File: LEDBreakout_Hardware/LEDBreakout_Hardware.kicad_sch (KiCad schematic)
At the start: 17 parts

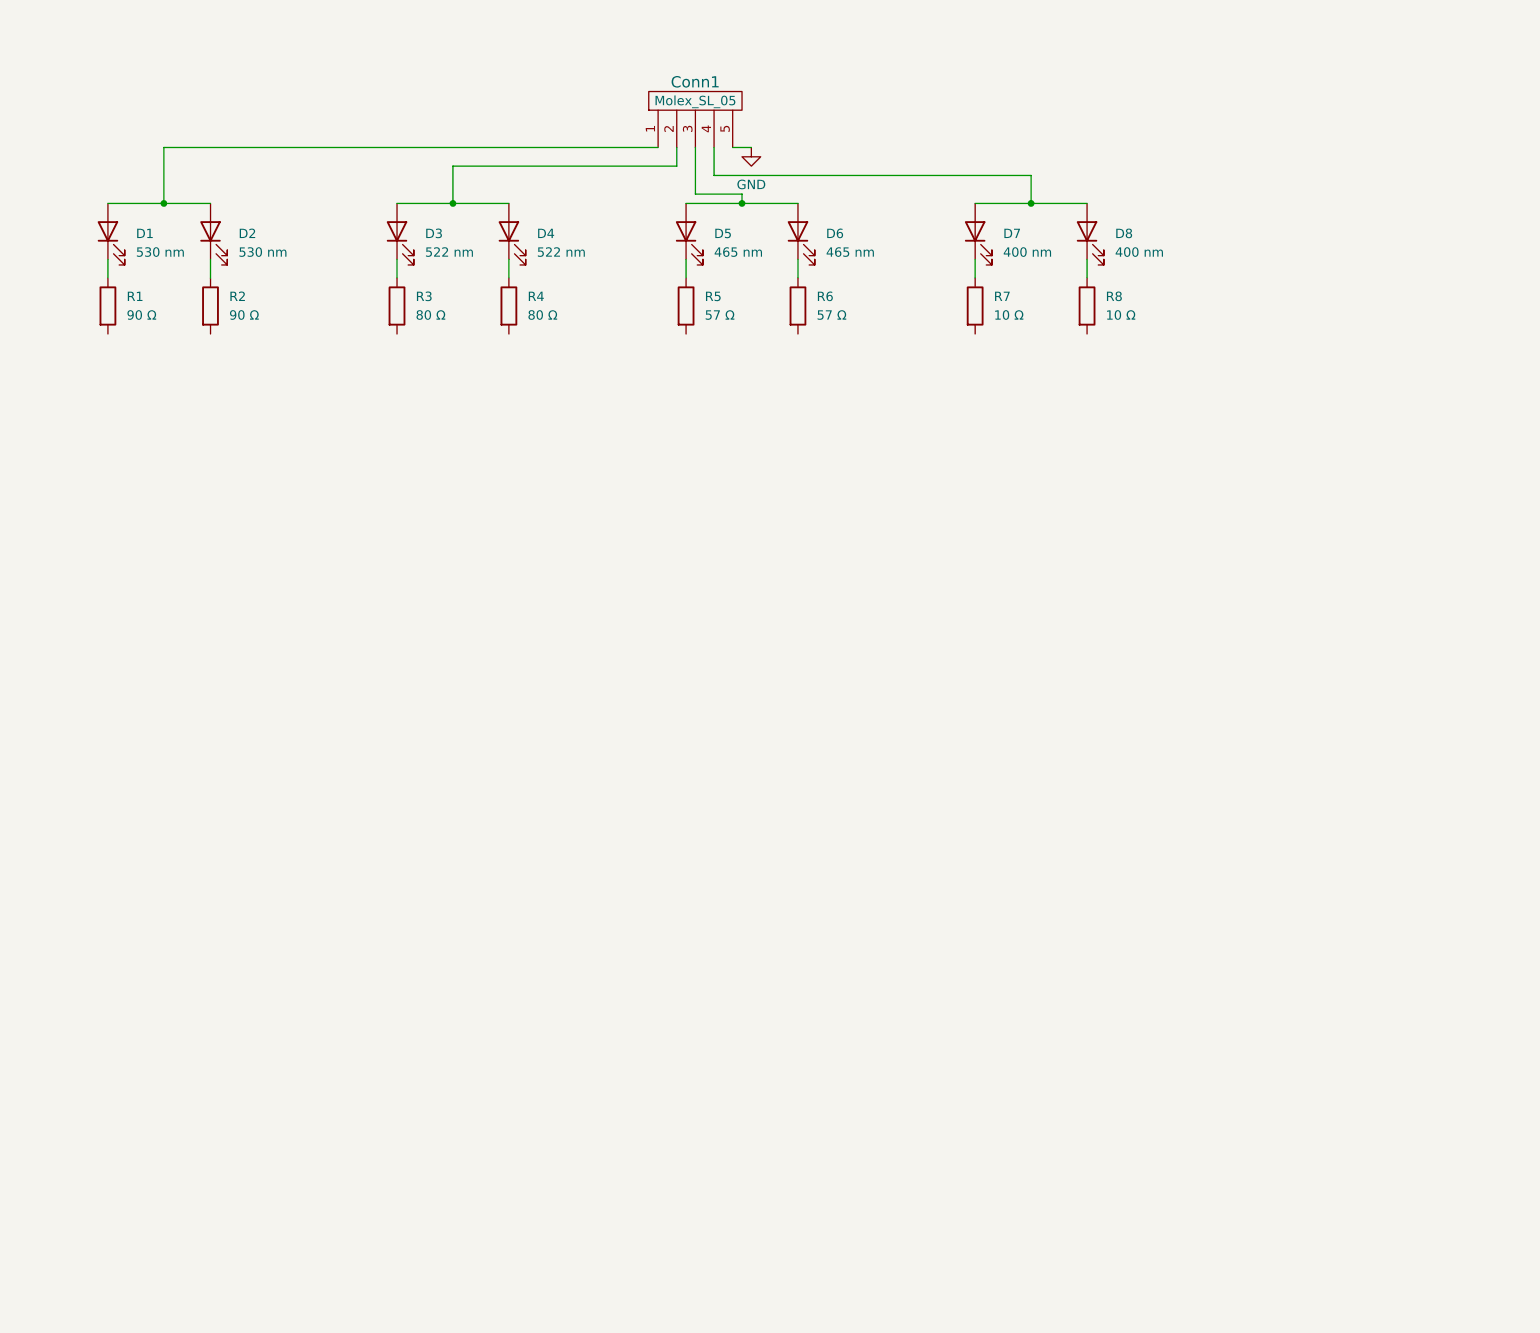
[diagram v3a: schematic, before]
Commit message: Added LED Breakout Connector to Fluoro Board
Also updated footprint for both boards
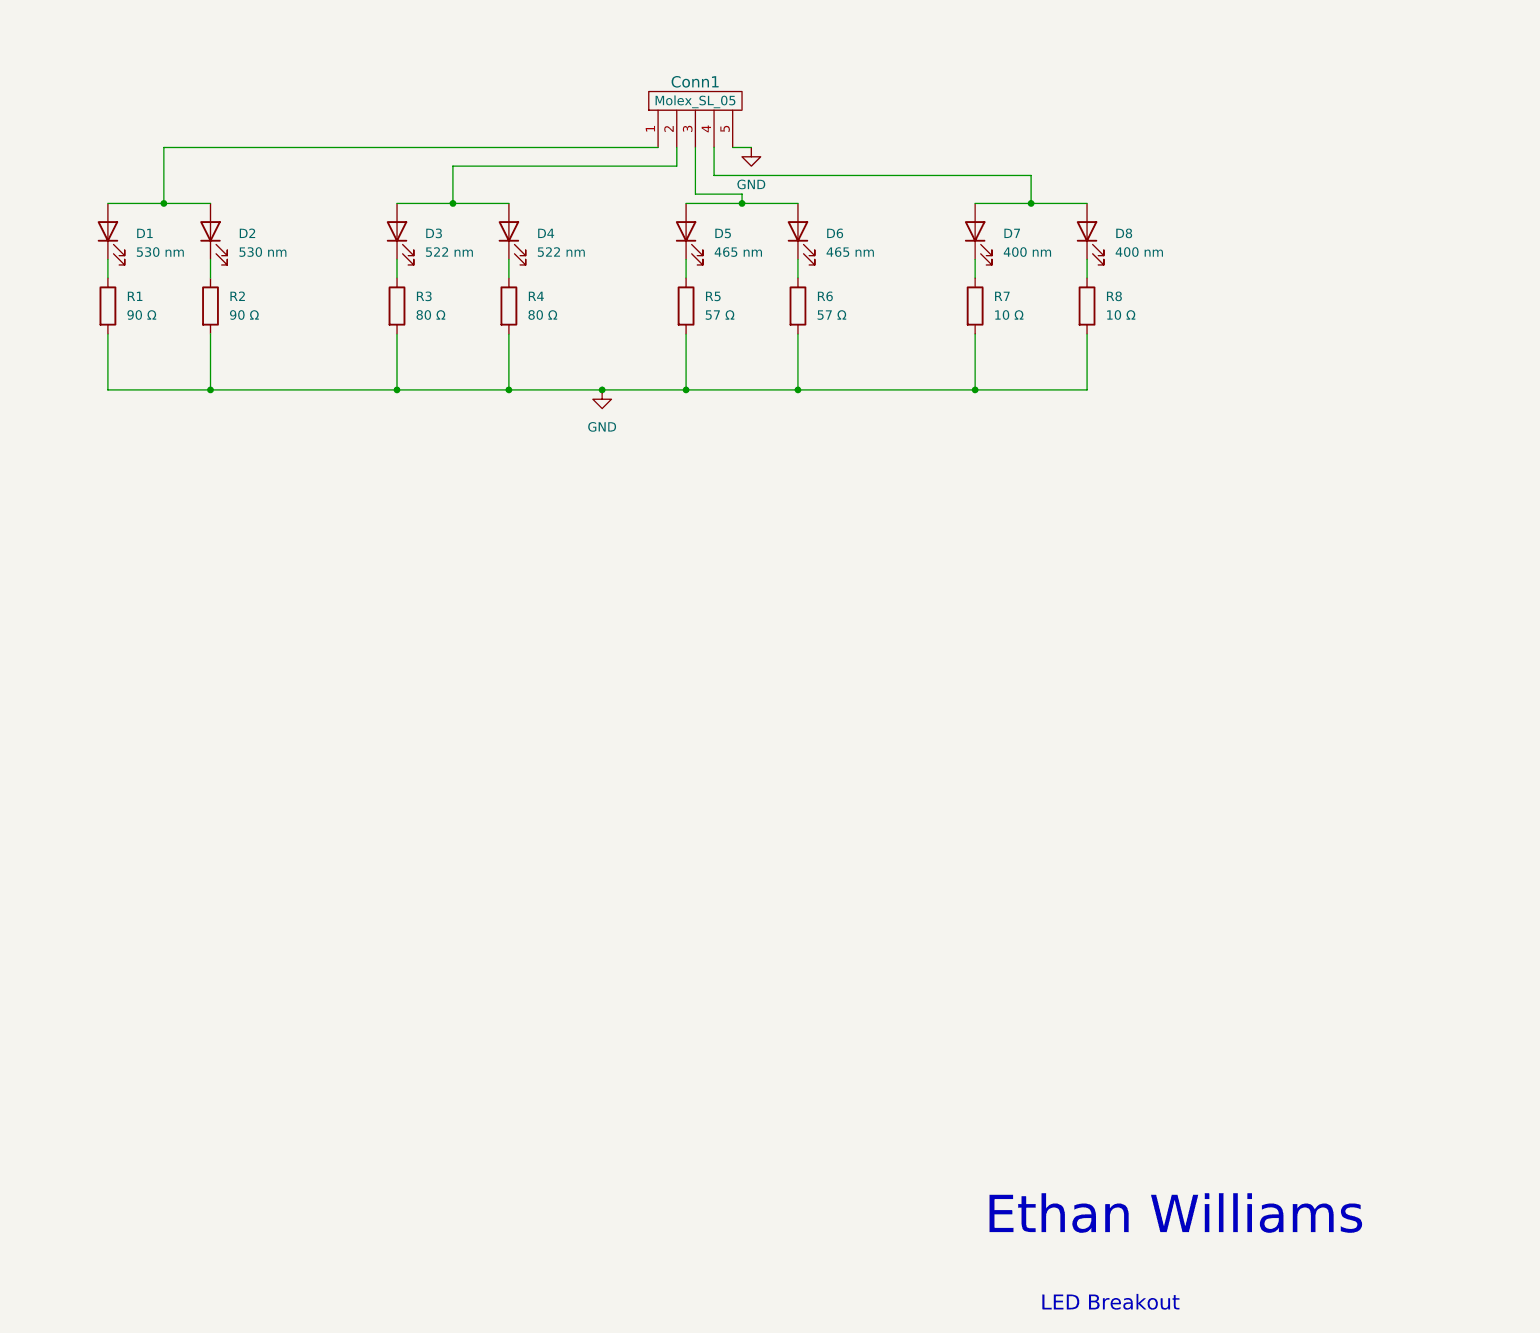
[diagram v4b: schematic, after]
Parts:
- Conn1: footprint (none) -> MRDT_Connectors:MOLEX_SL_05_Vertical
- D1, D2, D3, D4, D5, D6: footprint (none) -> Diode_THT:D_DO-15_P2.54mm_Vertical_AnodeUp
- D7, D8: footprint (none) -> MRDT_Passives:3528SMD_Diode
- R1, R2, R3, R4, R5, R6, R7, R8: footprint (none) -> Resistor_SMD:R_0603_1608Metric_Pad0.98x0.95mm_HandSolder
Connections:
- net GND: now also R1.2, R2.2, R3.2, R4.2, R5.2, R6.2, R7.2, R8.2
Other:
- note added: "Ethan Williams"
- note added: "LED Breakout"
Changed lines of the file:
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@@
 (kicad_sch (version 20230121) (generator eeschema)
   (paper "A4")
+  (junction (at 152.4 66.04) (diameter 0) (color 0 0 0 0)
+  )
   (junction (at 105.41 40.64) (diameter 0) (color 0 0 0 0)
   )
+  (junction (at 137.16 66.04) (diameter 0) (color 0 0 0 0)
+  )
+  (junction (at 97.79 66.04) (diameter 0) (color 0 0 0 0)
+  )
+  (junction (at 125.73 66.04) (diameter 0) (color 0 0 0 0)
+  )
   (junction (at 144.78 40.64) (diameter 0) (color 0 0 0 0)
   )
   (junction (at 184.15 40.64) (diameter 0) (color 0 0 0 0)
   )
+  (junction (at 72.39 66.04) (diameter 0) (color 0 0 0 0)
+  )
   (junction (at 66.04 40.64) (diameter 0) (color 0 0 0 0)
   )
+  (junction (at 176.53 66.04) (diameter 0) (color 0 0 0 0)
+  )
+  (junction (at 113.03 66.04) (diameter 0) (color 0 0 0 0)
+  )
   (wire (pts (xy 138.43 33.02) (xy 138.43 39.37))
     (stroke (width 0) (type default))
@@
     (stroke (width 0) (type default))
   )
+  (wire (pts (xy 113.03 58.42) (xy 113.03 66.04))
+    (stroke (width 0) (type default))
+  )
   (wire (pts (xy 191.77 48.26) (xy 191.77 50.8))
     (stroke (width 0) (type default))
   )
+  (wire (pts (xy 152.4 58.42) (xy 152.4 66.04))
+    (stroke (width 0) (type default))
+  )
   (wire (pts (xy 137.16 48.26) (xy 137.16 50.8))
     (stroke (width 0) (type default))
   )
+  (wire (pts (xy 97.79 66.04) (xy 113.03 66.04))
+    (stroke (width 0) (type default))
+  )
   (wire (pts (xy 113.03 48.26) (xy 113.03 50.8))
     (stroke (width 0) (type default))
@@
     (stroke (width 0) (type default))
   )
+  (wire (pts (xy 58.42 66.04) (xy 72.39 66.04))
+    (stroke (width 0) (type default))
+  )
   (wire (pts (xy 152.4 48.26) (xy 152.4 50.8))
     (stroke (width 0) (type default))
@@
     (stroke (width 0) (type default))
   )
+  (wire (pts (xy 72.39 66.04) (xy 97.79 66.04))
+    (stroke (width 0) (type default))
+  )
   (wire (pts (xy 97.79 48.26) (xy 97.79 50.8))
     (stroke (width 0) (type default))
@@
     (stroke (width 0) (type default))
   )
+  (wire (pts (xy 176.53 66.04) (xy 191.77 66.04))
+    (stroke (width 0) (type default))
+  )
+  (wire (pts (xy 97.79 58.42) (xy 97.79 66.04))
+    (stroke (width 0) (type default))
+  )
   (wire (pts (xy 143.51 33.02) (xy 146.05 33.02))
     (stroke (width 0) (type default))
@@
     (stroke (width 0) (type default))
   )
+  (wire (pts (xy 113.03 66.04) (xy 125.73 66.04))
+    (stroke (width 0) (type default))
+  )
+  (wire (pts (xy 137.16 58.42) (xy 137.16 66.04))
+    (stroke (width 0) (type default))
+  )
+  (wire (pts (xy 176.53 58.42) (xy 176.53 66.04))
+    (stroke (width 0) (type default))
+  )
+  (wire (pts (xy 58.42 58.42) (xy 58.42 66.04))
+    (stroke (width 0) (type default))
+  )
+  (wire (pts (xy 191.77 66.04) (xy 191.77 58.42))
+    (stroke (width 0) (type default))
+  )
   (wire (pts (xy 58.42 48.26) (xy 58.42 50.8))
     (stroke (width 0) (type default))
@@
     (stroke (width 0) (type default))
   )
+  (wire (pts (xy 125.73 66.04) (xy 137.16 66.04))
+    (stroke (width 0) (type default))
+  )
   (wire (pts (xy 105.41 40.64) (xy 113.03 40.64))
     (stroke (width 0) (type default))
   )
+  (wire (pts (xy 152.4 66.04) (xy 176.53 66.04))
+    (stroke (width 0) (type default))
+  )
   (wire (pts (xy 135.89 33.02) (xy 135.89 35.56))
     (stroke (width 0) (type default))
@@
     (stroke (width 0) (type default))
   )
+  (wire (pts (xy 72.39 58.42) (xy 72.39 66.04))
+    (stroke (width 0) (type default))
+  )
+  (wire (pts (xy 137.16 66.04) (xy 152.4 66.04))
+    (stroke (width 0) (type default))
+  )
   (wire (pts (xy 72.39 48.26) (xy 72.39 50.8))
     (stroke (width 0) (type default))
+  )
+  (text "LED Breakout" (at 185.42 191.77 0)
+    (effects (font (size 2.032 2.032)) (justify left bottom))
+  )
+  (text "Ethan Williams" (at 177.8 181.61 0)
+    (effects (font (size 5.08 5.08)) (justify left bottom))
   )
   (symbol (lib_id "Device:LED") (at 137.16 44.45 90) (unit 1)
@@
       (effects (font (size 1.27 1.27)) (justify right))
     )
-    (property "Footprint" "" (at 137.16 44.45 0)
+    (property "Footprint" "Diode_THT:D_DO-15_P2.54mm_Vertical_AnodeUp" (at 137.16 44.45 0)
       (effects (font (size 1.27 1.27)) hide)
     )
@@
       (effects (font (size 1.27 1.27)) (justify left))
     )
-    (property "Footprint" "" (at 174.752 54.61 90)
+    (property "Footprint" "Resistor_SMD:R_0603_1608Metric_Pad0.98x0.95mm_HandSolder" (at 174.752 54.61 90)
       (effects (font (size 1.27 1.27)) hide)
     )
@@
       (effects (font (size 1.27 1.27)) (justify left))
     )
-    (property "Footprint" "" (at 96.012 54.61 90)
+    (property "Footprint" "Resistor_SMD:R_0603_1608Metric_Pad0.98x0.95mm_HandSolder" (at 96.012 54.61 90)
       (effects (font (size 1.27 1.27)) hide)
     )
@@
       (effects (font (size 1.27 1.27)) (justify right))
     )
-    (property "Footprint" "" (at 176.53 44.45 0)
+    (property "Footprint" "MRDT_Passives:3528SMD_Diode" (at 176.53 44.45 0)
       (effects (font (size 1.27 1.27)) hide)
     )
@@
       (effects (font (size 1.27 1.27)) (justify left))
     )
-    (property "Footprint" "" (at 150.622 54.61 90)
+    (property "Footprint" "Resistor_SMD:R_0603_1608Metric_Pad0.98x0.95mm_HandSolder" (at 150.622 54.61 90)
       (effects (font (size 1.27 1.27)) hide)
     )
@@
       (effects (font (size 1.27 1.27)) (justify left))
     )
-    (property "Footprint" "" (at 189.992 54.61 90)
+    (property "Footprint" "Resistor_SMD:R_0603_1608Metric_Pad0.98x0.95mm_HandSolder" (at 189.992 54.61 90)
       (effects (font (size 1.27 1.27)) hide)
     )
@@
       (effects (font (size 1.27 1.27)) (justify right))
     )
-    (property "Footprint" "" (at 152.4 44.45 0)
+    (property "Footprint" "Diode_THT:D_DO-15_P2.54mm_Vertical_AnodeUp" (at 152.4 44.45 0)
       (effects (font (size 1.27 1.27)) hide)
     )
@@
       (effects (font (size 1.27 1.27)))
     )
-    (property "Footprint" "" (at 144.78 27.94 0)
+    (property "Footprint" "MRDT_Connectors:MOLEX_SL_05_Vertical" (at 144.78 27.94 0)
       (effects (font (size 1.524 1.524)) hide)
     )
@@
       (effects (font (size 1.27 1.27)) (justify right))
     )
-    (property "Footprint" "" (at 113.03 44.45 0)
+    (property "Footprint" "Diode_THT:D_DO-15_P2.54mm_Vertical_AnodeUp" (at 113.03 44.45 0)
       (effects (font (size 1.27 1.27)) hide)
     )
@@
     )
   )
+  (symbol (lib_id "power:GND") (at 125.73 66.04 0) (unit 1)
+    (in_bom yes) (on_board yes) (dnp no) (fields_autoplaced)
+    (property "Reference" "#PWR02" (at 125.73 72.39 0)
+      (effects (font (size 1.27 1.27)) hide)
+    )
+    (property "Value" "GND" (at 125.73 71.12 0)
+      (effects (font (size 1.27 1.27)))
+    )
+    (property "Footprint" "" (at 125.73 66.04 0)
+      (effects (font (size 1.27 1.27)) hide)
+    )
+    (property "Datasheet" "" (at 125.73 66.04 0)
+      (effects (font (size 1.27 1.27)) hide)
+    )
+    (pin "1")
+    (instances
+      (project "LEDBreakout_Hardware"
+        (path "/ab470af1-6cd3-447b-a747-284931828d17"
+          (reference "#PWR02") (unit 1)
+        )
+      )
+    )
+  )
   (symbol (lib_id "Device:R") (at 72.39 54.61 0) (unit 1)
     (in_bom yes) (on_board yes) (dnp no) (fields_autoplaced)
@@
       (effects (font (size 1.27 1.27)) (justify left))
     )
-    (property "Footprint" "" (at 70.612 54.61 90)
+    (property "Footprint" "Resistor_SMD:R_0603_1608Metric_Pad0.98x0.95mm_HandSolder" (at 70.612 54.61 90)
       (effects (font (size 1.27 1.27)) hide)
     )
@@
       (effects (font (size 1.27 1.27)) (justify right))
     )
-    (property "Footprint" "" (at 191.77 44.45 0)
+    (property "Footprint" "MRDT_Passives:3528SMD_Diode" (at 191.77 44.45 0)
       (effects (font (size 1.27 1.27)) hide)
     )
@@
       (effects (font (size 1.27 1.27)) (justify left))
     )
-    (property "Footprint" "" (at 135.382 54.61 90)
+    (property "Footprint" "Resistor_SMD:R_0603_1608Metric_Pad0.98x0.95mm_HandSolder" (at 135.382 54.61 90)
       (effects (font (size 1.27 1.27)) hide)
     )
@@
       (effects (font (size 1.27 1.27)) (justify left))
     )
-    (property "Footprint" "" (at 111.252 54.61 90)
+    (property "Footprint" "Resistor_SMD:R_0603_1608Metric_Pad0.98x0.95mm_HandSolder" (at 111.252 54.61 90)
       (effects (font (size 1.27 1.27)) hide)
     )
@@
       (effects (font (size 1.27 1.27)) (justify left))
     )
-    (property "Footprint" "" (at 56.642 54.61 90)
+    (property "Footprint" "Resistor_SMD:R_0603_1608Metric_Pad0.98x0.95mm_HandSolder" (at 56.642 54.61 90)
       (effects (font (size 1.27 1.27)) hide)
     )
@@
       (effects (font (size 1.27 1.27)) (justify right))
     )
-    (property "Footprint" "" (at 97.79 44.45 0)
+    (property "Footprint" "Diode_THT:D_DO-15_P2.54mm_Vertical_AnodeUp" (at 97.79 44.45 0)
       (effects (font (size 1.27 1.27)) hide)
     )
@@
       (effects (font (size 1.27 1.27)) (justify right))
     )
-    (property "Footprint" "" (at 58.42 44.45 0)
+    (property "Footprint" "Diode_THT:D_DO-15_P2.54mm_Vertical_AnodeUp" (at 58.42 44.45 0)
       (effects (font (size 1.27 1.27)) hide)
     )
@@
       (effects (font (size 1.27 1.27)) (justify right))
     )
-    (property "Footprint" "" (at 72.39 44.45 0)
-      (effects (font (size 1.27 1.27)) hide)
-    )
+    (property "Footprint" "Diode_THT:D_DO-15_P2.54mm_Vertical_AnodeUp" (at 72.39 44.45 0)
+      (effects (font (size 1.27 1.27)) hide)
+    )
